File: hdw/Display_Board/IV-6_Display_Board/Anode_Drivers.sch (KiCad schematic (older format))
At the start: 48 parts, among them Q201 PMSTA06, Q202 PMSTA06, Q203 BC856W, Q204 BC856W, Q205 PMSTA06, Q206 PMSTA06, Q207 BC856W, Q208 BC856W, Q209 PMSTA06, Q210 PMSTA06, Q211 BC856W, Q212 BC856W, Q213 PMSTA06, Q214 PMSTA06, Q215 BC856W, Q216 BC856W

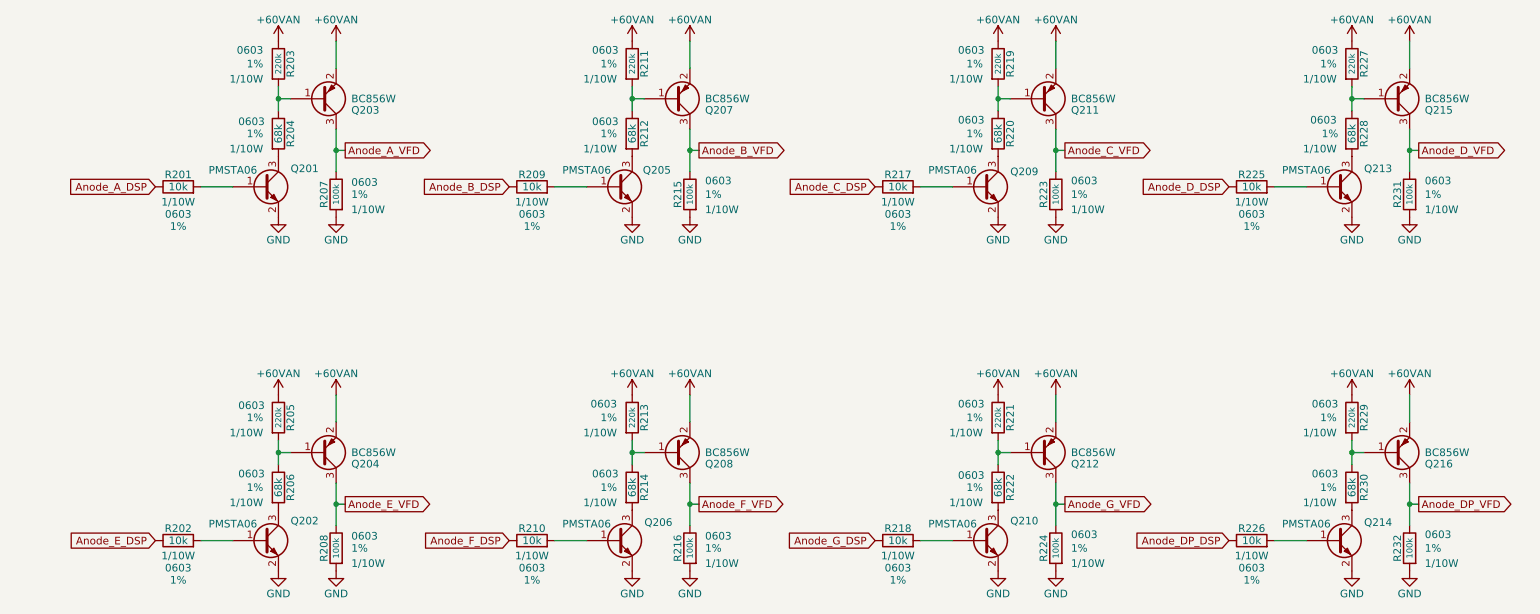
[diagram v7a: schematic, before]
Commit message: refactored a lot of display board stuff
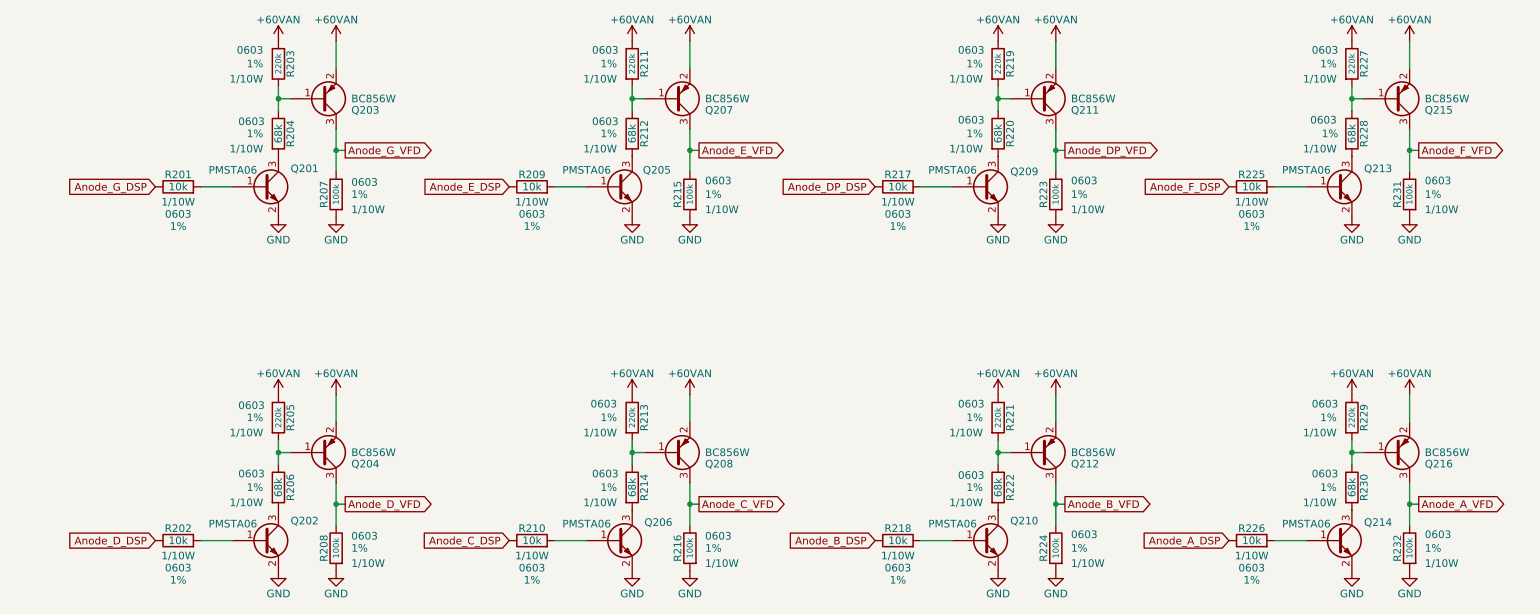
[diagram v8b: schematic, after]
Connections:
- net Anode_A_DSP: now also R226.1; no longer R201.1
- net Anode_A_VFD: now also Q216.3 (C), R232.1; no longer Q203.3 (C), R207.1
- net Anode_B_DSP: now also R218.1; no longer R209.1
- net Anode_B_VFD: now also Q212.3 (C), R224.1; no longer Q207.3 (C), R215.1
- net Anode_C_DSP: now also R210.1; no longer R217.1
- net Anode_C_VFD: now also Q208.3 (C), R216.1; no longer Q211.3 (C), R223.1
- net Anode_DP_DSP: now also R217.1; no longer R226.1
- net Anode_DP_VFD: now also Q211.3 (C), R223.1; no longer Q216.3 (C), R232.1
- net Anode_D_DSP: now also R202.1; no longer R225.1
- net Anode_D_VFD: now also Q204.3 (C), R208.1; no longer Q215.3 (C), R231.1
- net Anode_E_DSP: now also R209.1; no longer R202.1
- net Anode_E_VFD: now also Q207.3 (C), R215.1; no longer Q204.3 (C), R208.1
- net Anode_F_DSP: now also R225.1; no longer R210.1
- net Anode_F_VFD: now also Q215.3 (C), R231.1; no longer Q208.3 (C), R216.1
- net Anode_G_DSP: now also R201.1; no longer R218.1
- net Anode_G_VFD: now also Q203.3 (C), R207.1; no longer Q212.3 (C), R224.1
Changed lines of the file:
@@
 	1800 2500 1590 2500
 Text GLabel 1290 2500 0    50   Input ~ 0
+Anode_G_DSP
+Text GLabel 3620 2500 0    50   Input ~ 0
+Anode_E_DSP
+Text GLabel 6030 2500 0    50   Input ~ 0
+Anode_DP_DSP
+Text GLabel 8360 2500 0    50   Input ~ 0
+Anode_F_DSP
+Text GLabel 1290 4830 0    50   Input ~ 0
+Anode_D_DSP
+Text GLabel 3620 4830 0    50   Input ~ 0
+Anode_C_DSP
+Text GLabel 6030 4830 0    50   Input ~ 0
+Anode_B_DSP
+Text GLabel 8360 4830 0    50   Input ~ 0
 Anode_A_DSP
-Text GLabel 3620 2500 0    50   Input ~ 0
-Anode_B_DSP
-Text GLabel 6030 2500 0    50   Input ~ 0
-Anode_C_DSP
-Text GLabel 8360 2500 0    50   Input ~ 0
-Anode_D_DSP
-Text GLabel 1290 4830 0    50   Input ~ 0
-Anode_E_DSP
-Text GLabel 3620 4830 0    50   Input ~ 0
-Anode_F_DSP
-Text GLabel 6030 4830 0    50   Input ~ 0
-Anode_G_DSP
-Text GLabel 8360 4830 0    50   Input ~ 0
-Anode_DP_DSP
 Wire Wire Line
 	2540 2260 2480 2260
@@
 	4130 2500 3920 2500
 Text GLabel 4870 2260 2    50   Output ~ 0
-Anode_B_VFD
+Anode_E_VFD
 Wire Wire Line
 	4870 2260 4810 2260
@@
 	6540 2500 6330 2500
 Text GLabel 7280 2260 2    50   Output ~ 0
-Anode_C_VFD
+Anode_DP_VFD
 Wire Wire Line
 	7280 2260 7220 2260
@@
 	8870 2500 8660 2500
 Text GLabel 9610 2260 2    50   Output ~ 0
-Anode_D_VFD
+Anode_F_VFD
 Wire Wire Line
 	9610 2260 9550 2260
@@
 	1800 4830 1590 4830
 Text GLabel 2540 4590 2    50   Output ~ 0
-Anode_E_VFD
+Anode_D_VFD
 Wire Wire Line
 	2540 4590 2480 4590
@@
 	6540 4830 6330 4830
 Text GLabel 7280 4590 2    50   Output ~ 0
-Anode_G_VFD
+Anode_B_VFD
 Wire Wire Line
 	7280 4590 7220 4590
@@
 	8870 4830 8660 4830
 Text GLabel 9610 4590 2    50   Output ~ 0
-Anode_DP_VFD
+Anode_A_VFD
 Wire Wire Line
 	9610 4590 9550 4590
@@
 	9550 4590 9550 4450
 Text GLabel 2540 2260 2    50   Output ~ 0
-Anode_A_VFD
+Anode_G_VFD
 $Comp
 L Custom_Library:+60VAN #PWR0201
@@
 $EndComp
 Text GLabel 4870 4590 2    50   Output ~ 0
-Anode_F_VFD
+Anode_C_VFD
 $EndSCHEMATC
